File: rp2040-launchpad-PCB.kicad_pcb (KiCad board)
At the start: 2 copper layers, 58.4 x 83.8 mm, 116 parts, among them J1 Target Isolation Jumpers, J10 DBG_PRGM, J11 UART_DBG, J12 DGB Exp. Header, J13 LED 0 EN, J2 LP Header left, J3 PWR Header, J4 LP Extension Heder, J5 LP Header right, J6 PWR Header, J7 Jumper, J8 LiPo 3,7V Batt., J9 PWR select, SW1 RESET, SW2 BOOT, U1 25Q32, U10 WS2812B-2020, U11 WS2812B-2020, U12 WS2812B-2020, U13 WS2812B-2020, U14 WS2812B-2020, U15 WS2812B-2020, U16 WS2812B-2020, U2 RP2040, U3 RS2299, U4 MCP73831, U5 XC9142B50C, U6 XC6220B33, U7 25Q32, U8 RP2040, U9 WS2812B-2020, Y1 12MHz, Y2 12MHz

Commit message: Changed Raspberry logo. Added more vias around LiPo charger.
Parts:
- removed the G*** at (133.6, 107.7)
- removed the G*** at (151.1, 101.3)
- added G***: LOGO, rp2040-launchpad-PCB:raspberry, B.Cu at (132.7, 109.3)
- added G***: LOGO, rp2040-launchpad-PCB:raspberry, F.Cu at (152.4, 102.0)
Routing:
- net GND_DBG: track 82.2 -> 86.0 mm, vias 50 -> 53

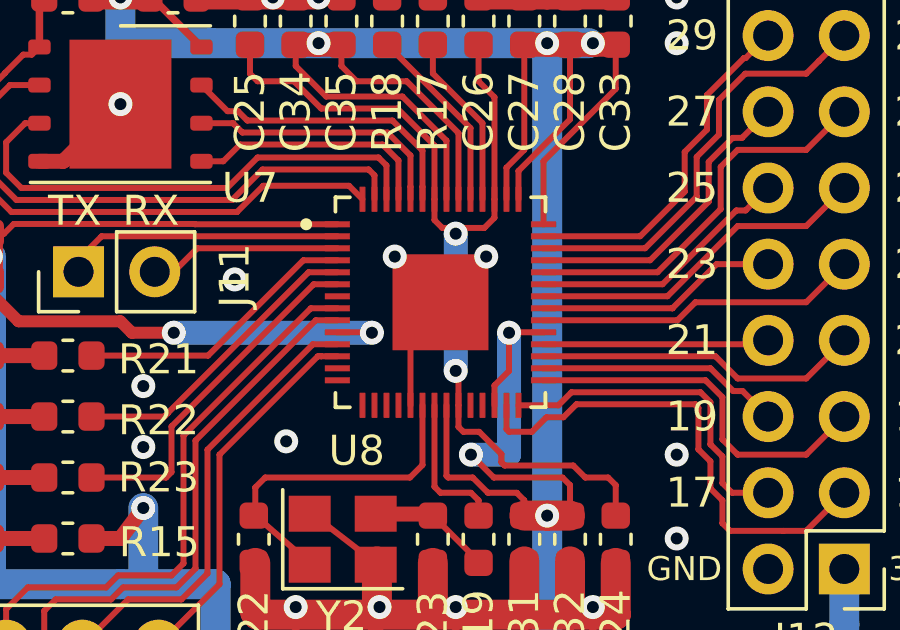
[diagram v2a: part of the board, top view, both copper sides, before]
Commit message: Small fix in layout below rp2040 (probe).
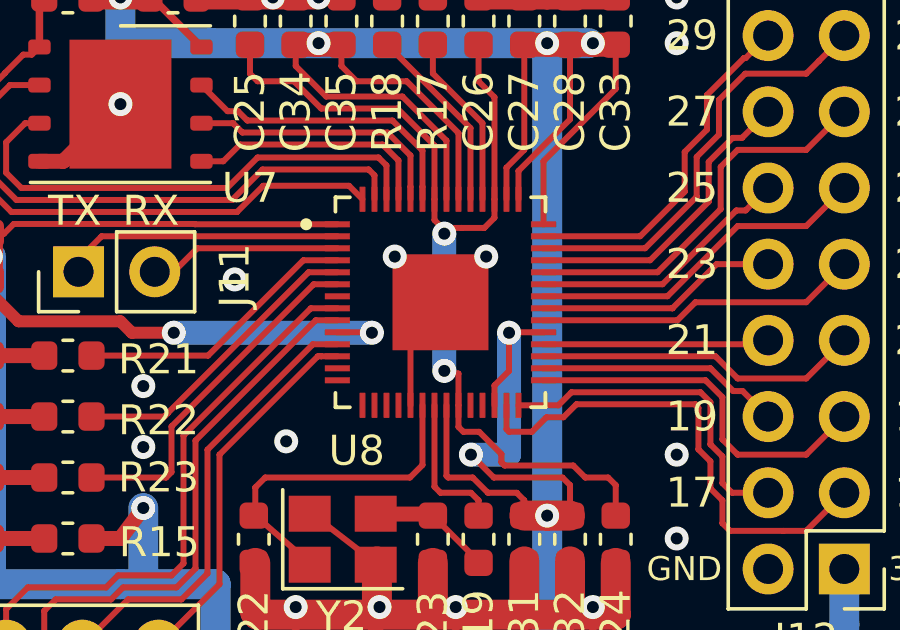
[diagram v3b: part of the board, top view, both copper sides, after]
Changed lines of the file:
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@@
     (thickness 1.6)
     (drawings 325)
-    (tracks 1909)
+    (tracks 1908)
     (zones 0)
     (modules 116)
@@
     (0 F.Cu signal)
     (31 B.Cu signal)
-    (32 B.Adhes user)
-    (33 F.Adhes user)
+    (32 B.Adhes user hide)
+    (33 F.Adhes user hide)
     (34 B.Paste user)
-    (35 F.Paste user)
-    (36 B.SilkS user)
-    (37 F.SilkS user)
+    (35 F.Paste user hide)
+    (36 B.SilkS user hide)
+    (37 F.SilkS user hide)
     (38 B.Mask user)
-    (39 F.Mask user)
+    (39 F.Mask user hide)
     (40 Dwgs.User user)
     (41 Cmts.User user)
@@
   )
   (setup
-    (last_trace_width 0.5)
+    (last_trace_width 0.25)
     (user_trace_width 0.2)
     (user_trace_width 0.4)
@@
   (segment (start 151.438 79.81) (end 151.699999 80.071999) (width 0.2) (layer F.Cu) (net 74))
   (segment (start 151.438 79.115) (end 151.438 79.81) (width 0.2) (layer F.Cu) (net 74))
-  (via (at 152.146 84.836) (size 0.8) (drill 0.4) (layers F.Cu B.Cu) (net 74))
-  (segment (start 152.238 84.928) (end 152.146 84.836) (width 0.2) (layer F.Cu) (net 74))
-  (segment (start 152.238 85.985) (end 152.238 84.928) (width 0.2) (layer F.Cu) (net 74))
-  (via (at 152.146 80.264) (size 0.8) (drill 0.4) (layers F.Cu B.Cu) (net 74))
-  (segment (start 152.146 84.836) (end 152.146 80.264) (width 0.8) (layer B.Cu) (net 74))
-  (segment (start 152.146 80.264) (end 152.338001 80.071999) (width 0.2) (layer F.Cu) (net 74))
   (segment (start 152.338001 80.071999) (end 153.100001 80.071999) (width 0.2) (layer F.Cu) (net 74))
   (segment (start 151.699999 80.071999) (end 152.338001 80.071999) (width 0.2) (layer F.Cu) (net 74))
@@
   (segment (start 145.288 74.93) (end 145.288 73.965) (width 0.2) (layer F.Cu) (net 74))
   (segment (start 145.542 75.184) (end 145.288 74.93) (width 0.2) (layer F.Cu) (net 74))
+  (segment (start 152.238 84.928) (end 152.238 85.985) (width 0.2) (layer F.Cu) (net 74))
+  (segment (start 151.765 84.836) (end 152.238 84.928) (width 0.2) (layer F.Cu) (net 74))
+  (via (at 151.765 84.836) (size 0.8) (drill 0.4) (layers F.Cu B.Cu) (net 74))
+  (segment (start 151.765 84.836) (end 151.765 80.264) (width 0.8) (layer B.Cu) (net 74))
+  (via (at 151.765 80.264) (size 0.8) (drill 0.4) (layers F.Cu B.Cu) (net 74))
   (segment (start 128.778 79.375) (end 128.778 77.724) (width 0.8) (layer F.Cu) (net 75))
   (segment (start 136.652 84.328) (end 138.43 84.328) (width 0.5) (layer F.Cu) (net 76))

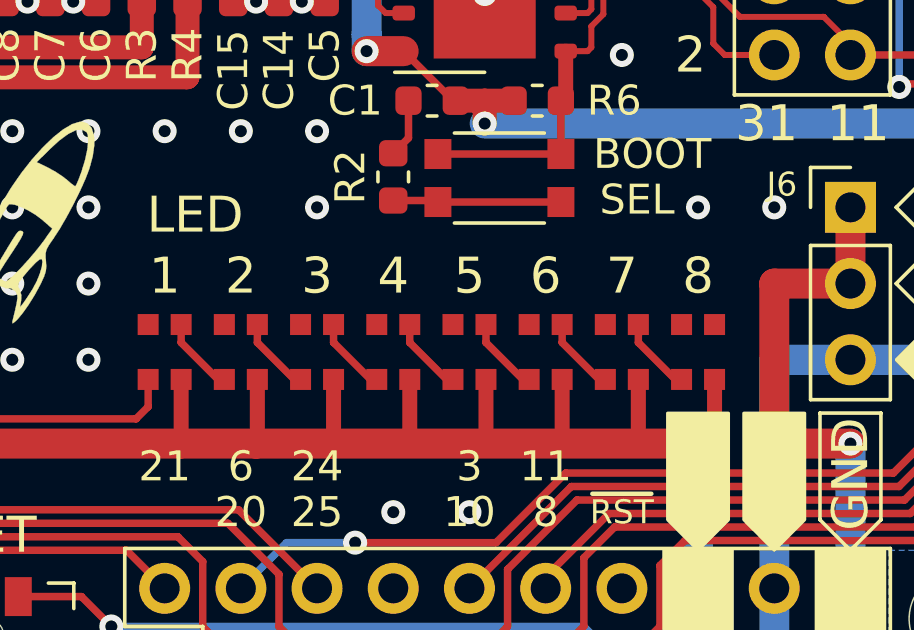
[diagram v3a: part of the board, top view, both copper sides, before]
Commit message: Added Pin1 silk for WS2812-2020 footprint. Generated new pos-Files because U9-U16 were missing.
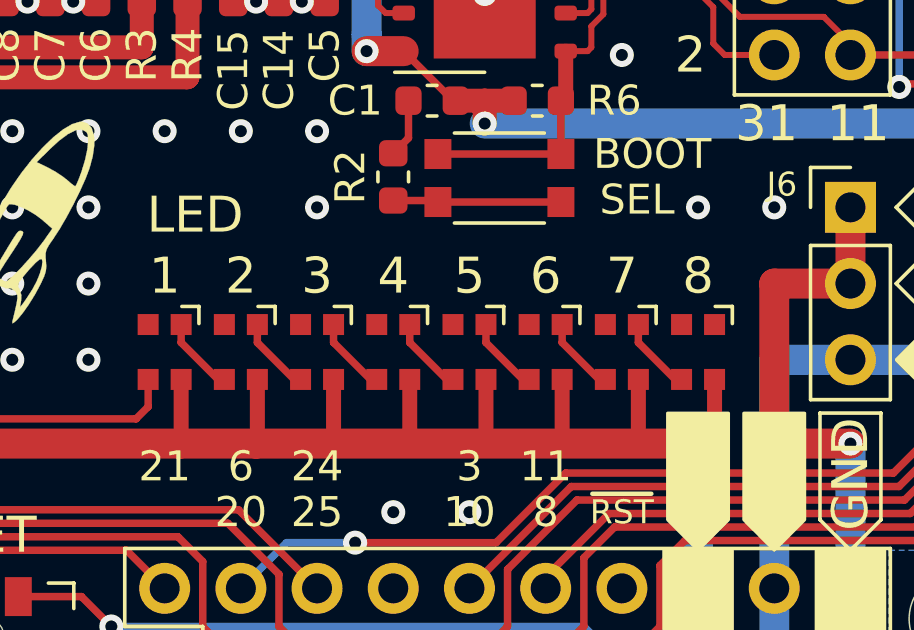
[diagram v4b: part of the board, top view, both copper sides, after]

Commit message: New version 1.3 - first commit
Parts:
- removed D4, D5: D_Schottky, Diode_SMD:D_SOD-123
- removed J9: PWR select, Connector_PinHeader_2.54mm:PinHeader_1x03_P2.54mm_Vertical
- added SW3: Switch_SP3T, rp2040-launchpad-PCB:PCM13SMTR, F.Cu at (112.6, 83.6)
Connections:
- C16 pad 2: +5V_DBG -> /DebugProbe/VBUS_DBG
- D3 pad 2: +5V_DBG -> /DebugProbe/VBUS_DBG
- J13 pad 1: /Target/ADC_7 -> /Target/SPI0_RX
- J4 pad 13: /Target/~RESET -> /Target/GPIO6
- J4 pad 4: /Target/GPIO6 -> Net-(J4-Pad4)
- J4 pad 8: Net-(J4-Pad8) -> Net-(J4-Pad4)
- U4 pad 4: +5V_DBG -> /DebugProbe/VBUS_DBG
- USB2 pad 1: +5V_DBG -> /DebugProbe/VBUS_DBG
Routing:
- net /Target/SPI0_RX: track 23.2 -> 69.0 mm, vias 0 -> 2
- net +5V_DBG: track 57.5 -> 26.8 mm, vias 5 -> 1
- net /DebugProbe/VBUS_DBG: track 0.00 -> 30.2 mm, vias 0 -> 4
- net Net-(D5-Pad1): track 9.30 -> 0.00 mm
- net Net-(D4-Pad1): track 8.29 -> 0.00 mm
- net /PowerSupply/VBUS_TRGT: track 65.5 -> 72.3 mm
- net /Target/ADC_7: track 65.0 -> 58.4 mm
- net Net-(C18-Pad2): track 12.6 -> 6.05 mm, vias 2 -> 0
- net Net-(J4-Pad4): track 0.00 -> 6.13 mm
- net /Target/~RESET: track 123.4 -> 120.6 mm, vias 6 -> 7
- net /Target/GPIO6: track 69.3 -> 71.6 mm
- net Net-(J13-Pad2): track 8.45 -> 6.56 mm
- net GND_DBG: track 86.0 -> 85.6 mm, vias 53 -> 54
- net GND: vias 98 -> 100
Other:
- board text added: "BATT"
- board text added: "PC"
- board text added: "RP2040 Launchpad v1.3 © A. Terstegge"
- board text added: "TRGT"
- board text removed: "BATT."
- board text removed: "RP2040 Launchpad v1.2 © A. Terstegge"
- board text removed: "TARGET"

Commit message: Version v1.3 finalized. Ready for production!
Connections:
- J13 pad 1: /Target/SPI0_RX -> /Target/PWM6B
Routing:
- net /Target/SPI0_RX: track 69.0 -> 23.2 mm, vias 2 -> 0
- net /Target/PWM6B: track 22.1 -> 62.9 mm, vias 0 -> 2
- net GND: track 92.6 -> 90.4 mm, vias 100 -> 99

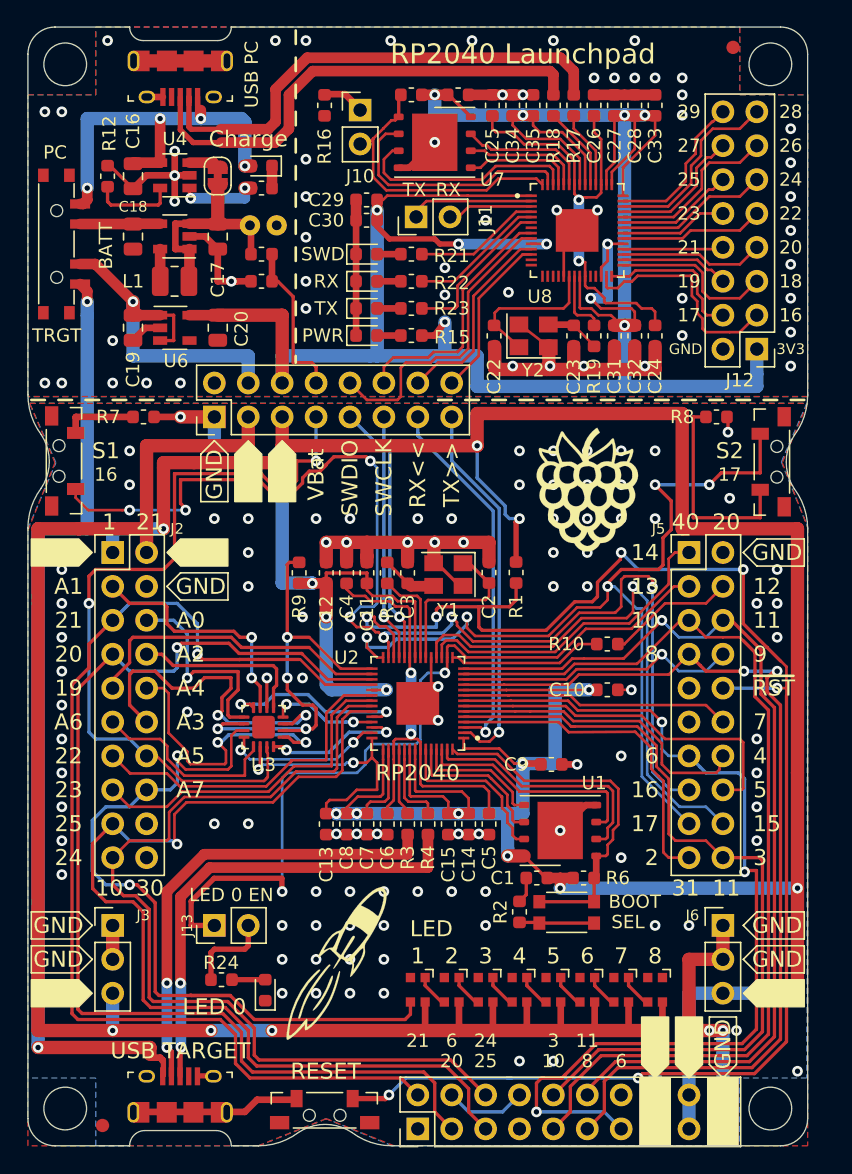
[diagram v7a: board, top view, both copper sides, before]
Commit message: Migration to KiCad version 8
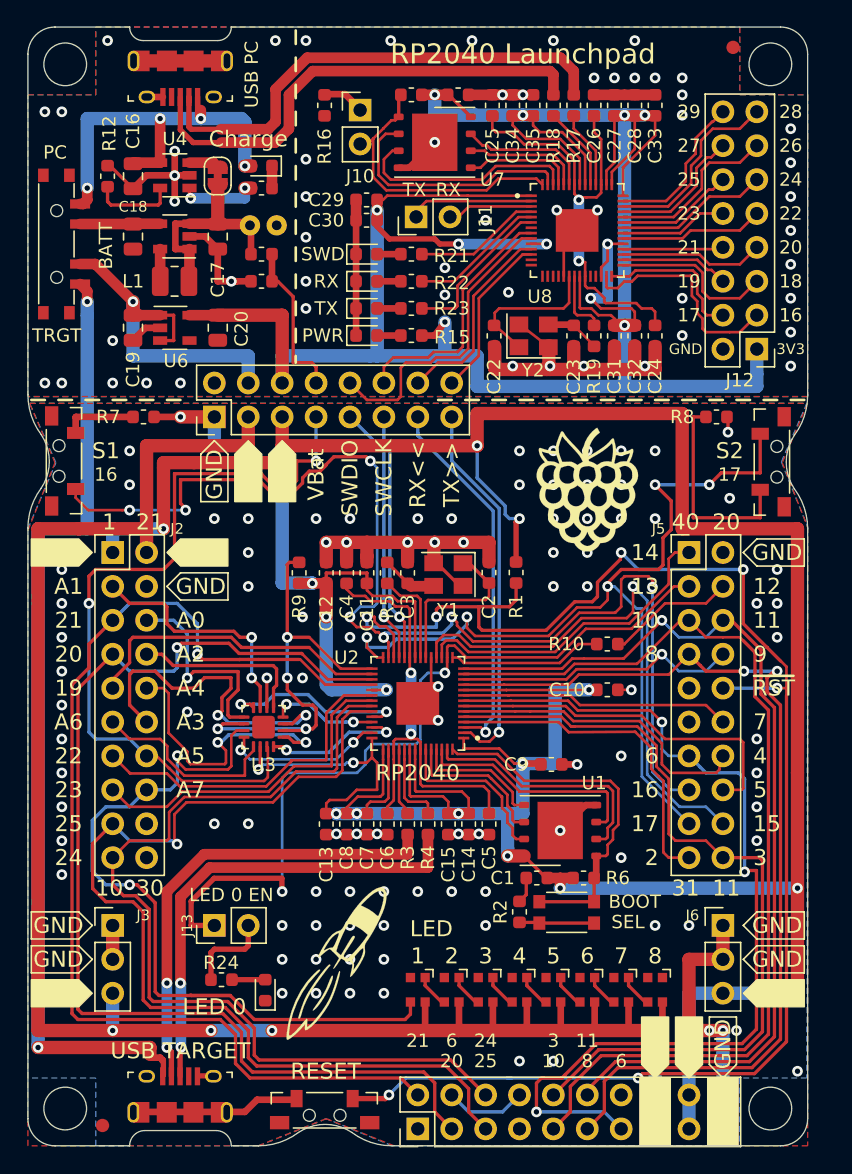
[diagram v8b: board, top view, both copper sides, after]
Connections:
- net /Target/~RESET renamed /Target/~{RESET}
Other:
- net class Default removed
- board text added: "~{RST}"
- board text removed: "~RST"
